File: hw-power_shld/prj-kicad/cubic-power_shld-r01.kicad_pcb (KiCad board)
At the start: 2 copper layers, 13.3 x 24.5 mm, 17 parts

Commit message: ...
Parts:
- moved Roc1 1.90 mm to (170.5, 89.4)
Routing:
- net GND: track 18.3 -> 21.4 mm, vias 5 -> 8
- net N-000002: track 11.3 -> 9.82 mm
- net N-000007: track 7.19 -> 5.88 mm
- net N-0000014: track 2.67 -> 3.52 mm
- net N-000001: track 5.84 -> 6.64 mm
- net N-0000013: track 7.69 -> 8.35 mm
- net N-000004: track 5.64 -> 6.27 mm

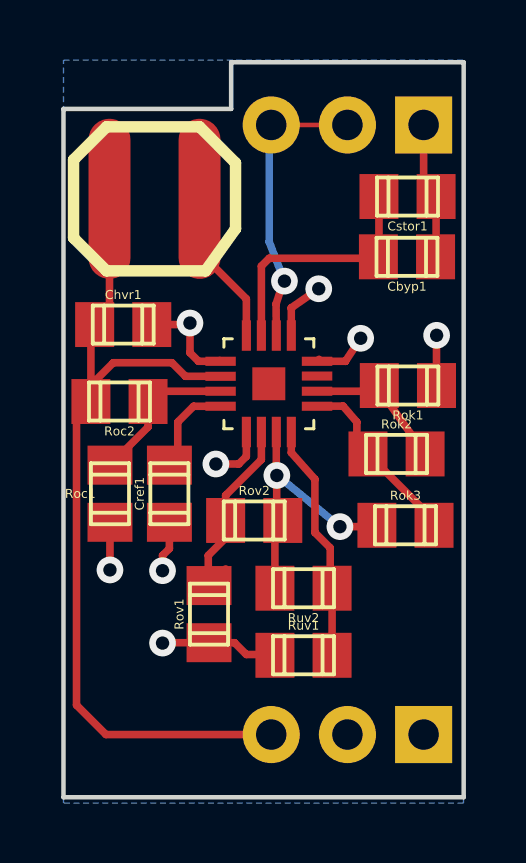
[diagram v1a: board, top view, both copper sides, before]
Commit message: add logo and move txt
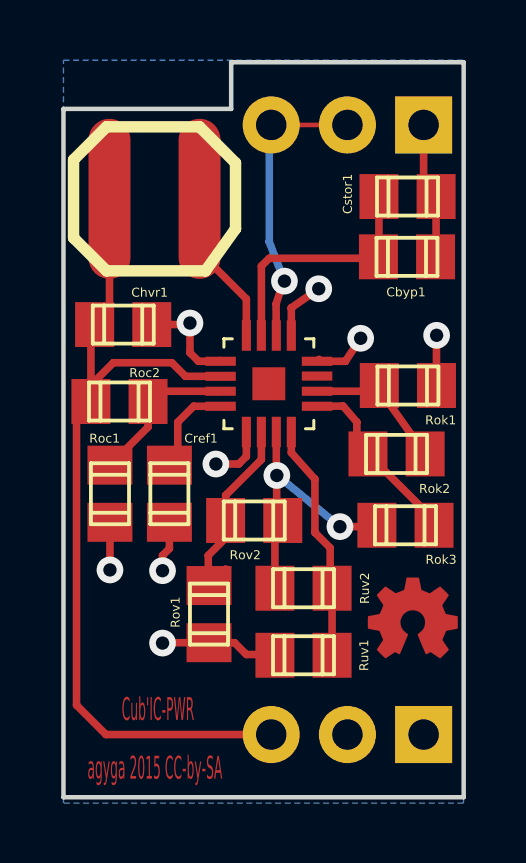
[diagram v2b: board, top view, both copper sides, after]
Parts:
- added G***: OSHW-logo_copper-back_3mm, OSHW-logo_copper-back_3mm, F.Cu at (180.6, 93.5)
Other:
- board text added: "Cub'IC-PWR"
- board text added: "agyga 2015 CC-by-SA"
